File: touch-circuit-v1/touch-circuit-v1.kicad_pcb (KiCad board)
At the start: 2 copper layers, 15.2 x 24.4 mm, 13 parts, among them J1 Conn_01x02, J2 Conn_01x02, U1 Opamp_Dual_Generic

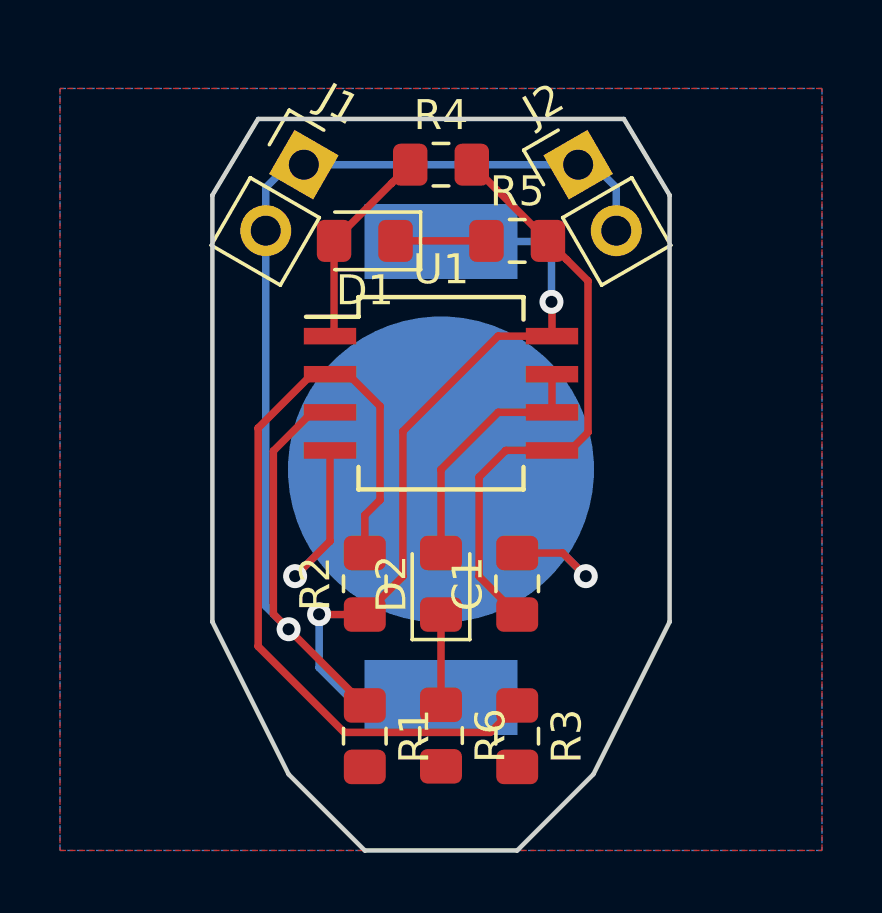
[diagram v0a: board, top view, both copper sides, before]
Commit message: add silk and update mounting footprints
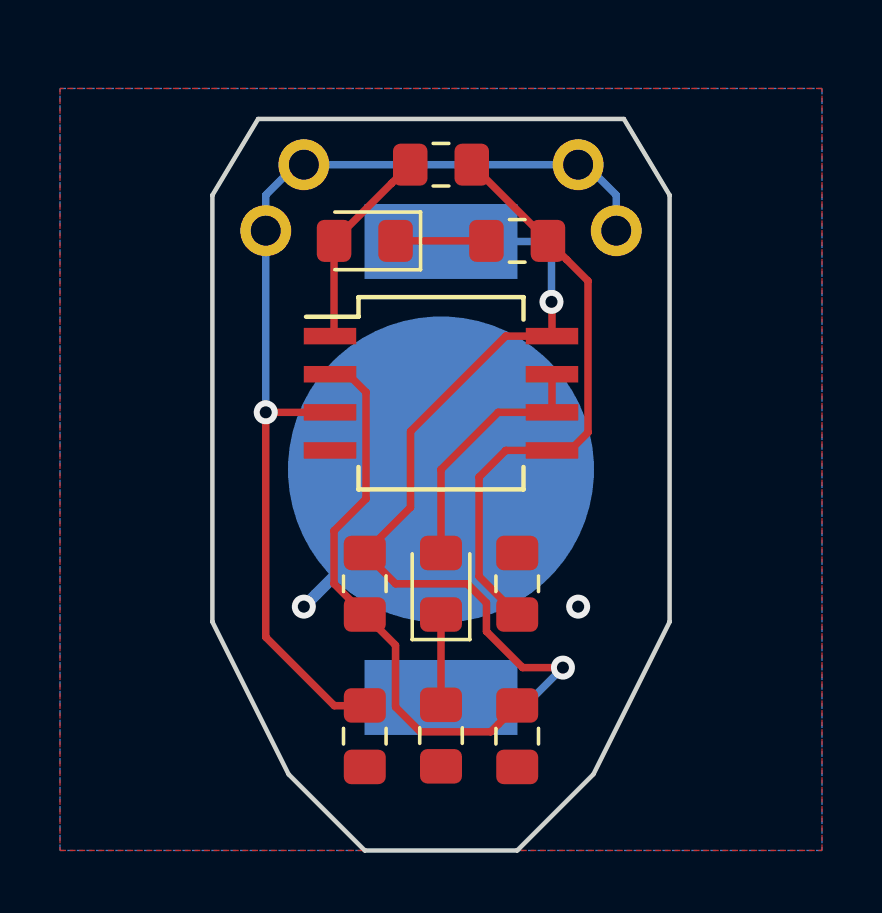
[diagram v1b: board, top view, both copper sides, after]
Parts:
- J1, J2: footprint Connector_PinHeader_2.54mm:PinHeader_1x02_P2.54mm_Vertical -> touch-circuit-v1:PinHeader_1x02_P2.54mm_Vertical_nosilk
- turned R2 to 270 degrees
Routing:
- net GND: track 19.9 -> 9.04 mm
- net Net-(R2-Pad2): track 27.8 -> 18.0 mm
- net /skin: track 41.0 -> 34.8 mm
- net +3V3: track 27.2 -> 30.4 mm
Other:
- board text added: "CC BY-NC-SA"
- board text added: "Tobin Yehle 2020/01/28"
- board text added: "Touch v1"
- board text added: "github.com/tyehle/touch-circuit"
